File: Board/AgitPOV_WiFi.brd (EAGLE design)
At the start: 37.4 x 69.6 mm, 40 parts, among them U1 MMA8452Q

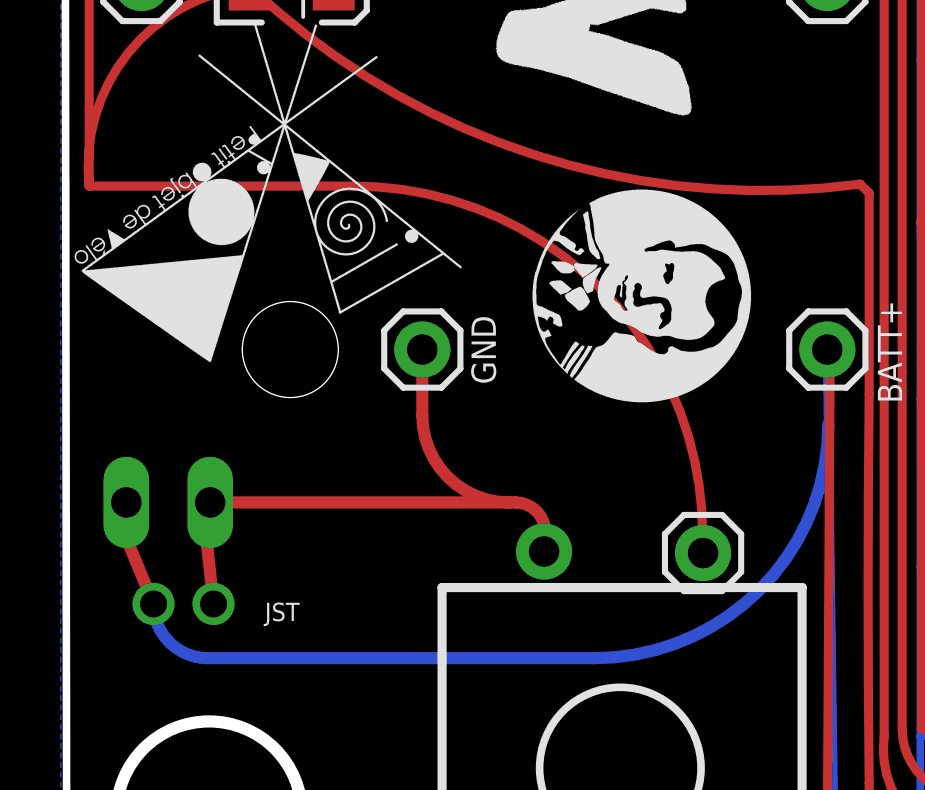
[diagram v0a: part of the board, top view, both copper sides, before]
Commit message: Cambios desde Manizales y Cartagena
- luz de colores en la pagina html
- individual AP desde el MAC address
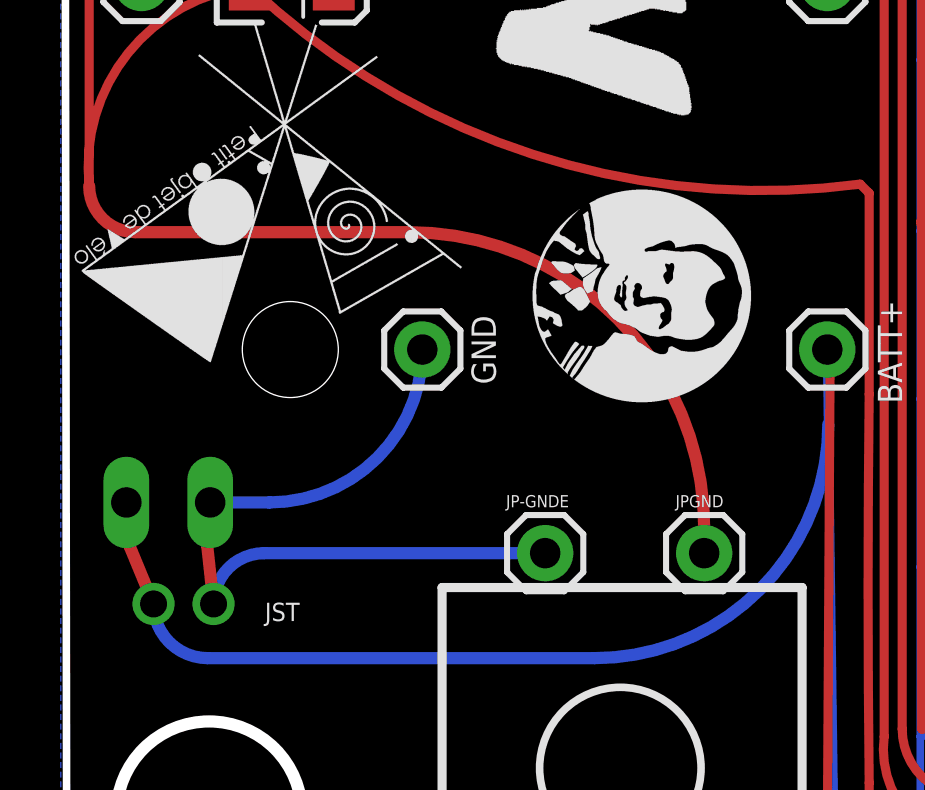
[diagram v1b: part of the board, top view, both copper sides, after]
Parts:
- removed JP-GND: SWITCH, SparkFun-Connectors:1X01
- added JPGND: switch, SparkFun-Connectors:1X01
- moved JP-GNDE 0.07 mm to (16.3, 13.9), flipped to the top
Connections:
- removed net GND1: JP-GND.1
- removed net N$65: U1.11
- removed net N$67: U1.9
- net ENTREEGND: now also JP-GNDE.1
- net GND: now also JPGND.1
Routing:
- net ENTREEGND: track 21.3 -> 24.3 mm
- net GND: track 394.7 -> 395.5 mm
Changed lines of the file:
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@@
 <layer number="17" name="Pads" color="2" fill="1" visible="yes" active="yes"/>
 <layer number="18" name="Vias" color="2" fill="1" visible="yes" active="yes"/>
-<layer number="19" name="Unrouted" color="6" fill="1" visible="yes" active="yes"/>
+<layer number="19" name="Unrouted" color="6" fill="1" visible="no" active="yes"/>
 <layer number="20" name="Dimension" color="15" fill="1" visible="yes" active="yes"/>
 <layer number="21" name="tPlace" color="14" fill="1" visible="yes" active="yes"/>
 <layer number="22" name="bPlace" color="13" fill="1" visible="yes" active="yes"/>
-<layer number="23" name="tOrigins" color="15" fill="1" visible="yes" active="yes"/>
-<layer number="24" name="bOrigins" color="15" fill="1" visible="yes" active="yes"/>
+<layer number="23" name="tOrigins" color="15" fill="1" visible="no" active="yes"/>
+<layer number="24" name="bOrigins" color="15" fill="1" visible="no" active="yes"/>
 <layer number="25" name="tNames" color="7" fill="1" visible="yes" active="yes"/>
-<layer number="26" name="bNames" color="7" fill="1" visible="yes" active="yes"/>
+<layer number="26" name="bNames" color="7" fill="1" visible="no" active="yes"/>
 <layer number="27" name="tValues" color="7" fill="1" visible="yes" active="yes"/>
-<layer number="28" name="bValues" color="7" fill="1" visible="yes" active="yes"/>
+<layer number="28" name="bValues" color="7" fill="1" visible="no" active="yes"/>
 <layer number="29" name="tStop" color="7" fill="3" visible="no" active="yes"/>
 <layer number="30" name="bStop" color="7" fill="6" visible="no" active="yes"/>
@@
 <element name="WEMOS2" library="SparkFun-Connectors" package="1X08_ROUND" value="Wemos D1 mini" x="2.84408125" y="50.6849625" smashed="yes" rot="R270">
 <attribute name="NAME" x="4.67288125" y="52.0311625" size="1.27" layer="25" ratio="10" rot="R270" display="off"/>
-<attribute name="VALUE" x="9.83608125" y="59.2519625" size="1.016" layer="28" rot="MR180"/>
+<attribute name="VALUE" x="9.83608125" y="59.2519625" size="1.016" layer="26" rot="MR180"/>
 </element>
 <element name="PIN0" library="SparkFun-Connectors" package="1X01" value="" x="25.80408125" y="2.4869625" smashed="yes">
@@
 <attribute name="VALUE" x="10.708" y="41.832" size="0.6096" layer="27" rot="SR0"/>
 </element>
-<element name="JP-GND" library="SparkFun-Connectors" package="1X01" value="SWITCH" x="21.5630375" y="13.90408125" smashed="yes" rot="R180">
-<attribute name="VALUE" x="23.6462375" y="10.44168125" size="0.8128" layer="26" rot="R270"/>
+<element name="JPGND" library="SparkFun-Connectors" package="1X01" value="switch" x="21.6" y="13.9" smashed="yes">
+<attribute name="NAME" x="20.6438" y="15.4288" size="0.4064" layer="25"/>
+<attribute name="VALUE" x="23.175" y="9.32" size="1.016" layer="27" rot="R270"/>
 </element>
-<element name="JP-GNDE" library="SparkFun-Connectors" package="1X01" value="" x="16.2630375" y="13.95408125" smashed="yes" rot="MR0">
-<attribute name="VALUE" x="17.5330375" y="10.77908125" size="1.27" layer="28" rot="MR0"/>
+<element name="JP-GNDE" library="SparkFun-Connectors" package="1X01" value="" x="16.3" y="13.9" smashed="yes">
+<attribute name="NAME" x="14.9938" y="15.4288" size="0.4064" layer="25"/>
+<attribute name="VALUE" x="15.03" y="10.725" size="1.27" layer="27"/>
 </element>
 </elements>
@@
 <wire x1="4.45" y1="49.75088125" x2="4.45" y2="52.82735625" width="0.4064" layer="1"/>
 <wire x1="4.45" y1="52.82735625" x2="5.00584375" y2="53.3832" width="0.4064" layer="1" curve="-90"/>
-<wire x1="1.1" y1="26.13548125" x2="9.91451875" y2="26.13548125" width="0.3048" layer="1"/>
-<wire x1="9.91451875" y1="26.13548125" x2="21.55" y2="14.5" width="0.3048" layer="1" curve="-90"/>
+<contactref element="JPGND" pad="1"/>
+<wire x1="1.1" y1="26.13548125" x2="2.63548125" y2="24.6" width="0.4064" layer="1" curve="90"/>
+<wire x1="2.63548125" y1="24.6" x2="11.75" y2="24.6" width="0.4064" layer="1"/>
+<wire x1="11.75" y1="24.6" x2="21.6" y2="14.75" width="0.4064" layer="1" curve="-90"/>
+<wire x1="21.6" y1="14.75" x2="21.6" y2="13.9" width="0.4064" layer="1"/>
 </signal>
 <signal name="N$6">
@@
 <wire x1="5.24511875" y1="12.2064375" x2="5.03251875" y2="14.1564375" width="0.4064" layer="1"/>
 <wire x1="5.03251875" y1="14.1564375" x2="5.13251875" y2="15.5904375" width="0.4064" layer="1"/>
-<wire x1="5.13251875" y1="15.5904375" x2="15.1" y2="15.5904375" width="0.4064" layer="1"/>
-<wire x1="15.1" y1="15.5904375" x2="15.3095625" y2="15.5904375" width="0.4064" layer="1"/>
-<wire x1="15.3095625" y1="15.5904375" x2="16.3" y2="14.6" width="0.4064" layer="1" curve="-90"/>
-<wire x1="12.20408125" y1="20.6869625" x2="12.20408125" y2="18.48635625" width="0.4064" layer="1"/>
-<wire x1="12.20408125" y1="18.48635625" x2="15.1" y2="15.5904375" width="0.4064" layer="1" curve="90"/>
+<contactref element="JP-GNDE" pad="1"/>
+<wire x1="12.20408125" y1="20.6869625" x2="7.10755625" y2="15.5904375" width="0.4064" layer="16" curve="-90"/>
+<wire x1="7.10755625" y1="15.5904375" x2="5.13251875" y2="15.5904375" width="0.4064" layer="16"/>
+<wire x1="5.24511875" y1="12.2064375" x2="6.93868125" y2="13.9" width="0.4064" layer="16" curve="-90"/>
+<wire x1="6.93868125" y1="13.9" x2="16.3" y2="13.9" width="0.4064" layer="16"/>
 </signal>
 <signal name="N$1">
@@
 <wire x1="17.8" y1="60.3" x2="25.70408125" y2="50.6849625" width="0.3048" layer="1" curve="-101.155894"/>
 </signal>
-<signal name="N$65">
-<contactref element="U1" pad="11"/>
-</signal>
-<signal name="N$67">
-<contactref element="U1" pad="9"/>
-</signal>
-<signal name="GND1">
-<contactref element="JP-GND" pad="1"/>
-</signal>
 </signals>

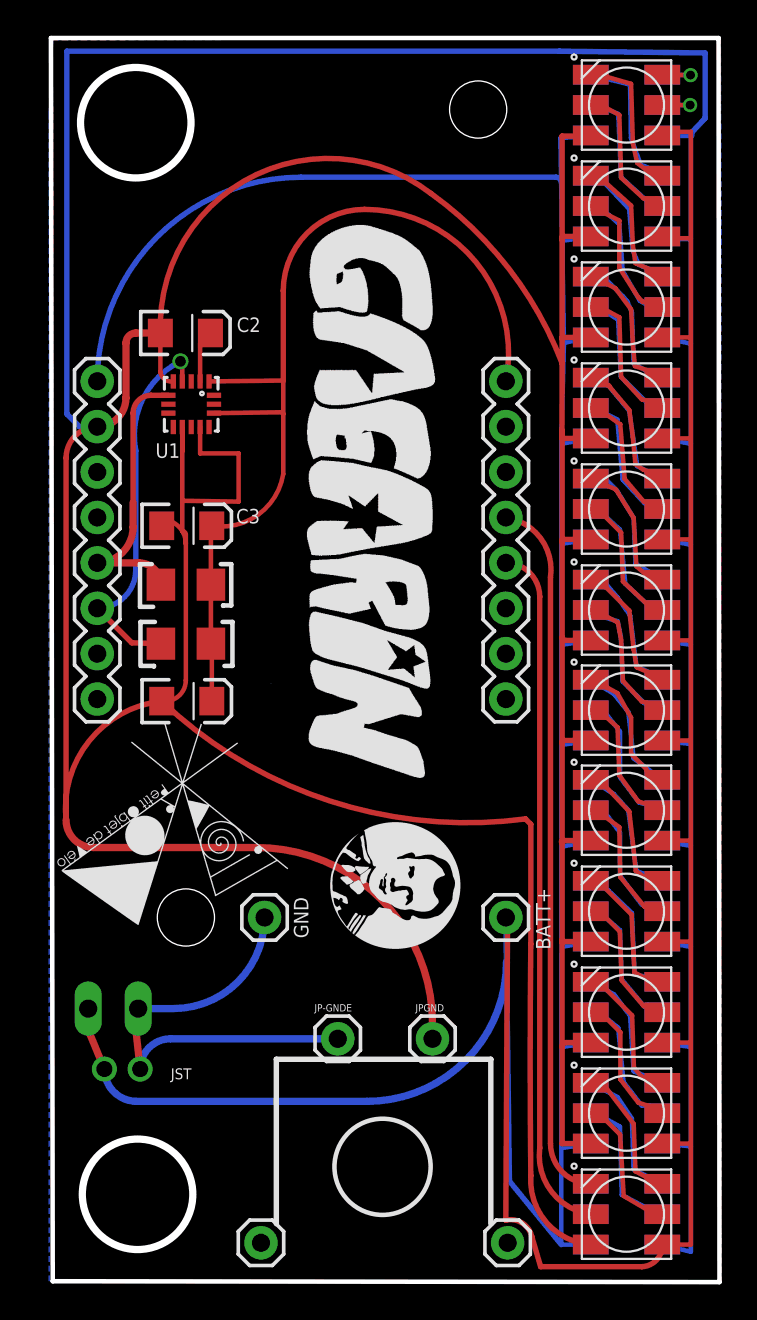
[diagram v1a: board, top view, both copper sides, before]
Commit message: Analysis and improvements to the lop
Implementation of spiffs accelerometer data saving (careful, there is a
200ms hit for every writing)
Scripts for gnuplot to analyze the data
Improvements to the low pass filter
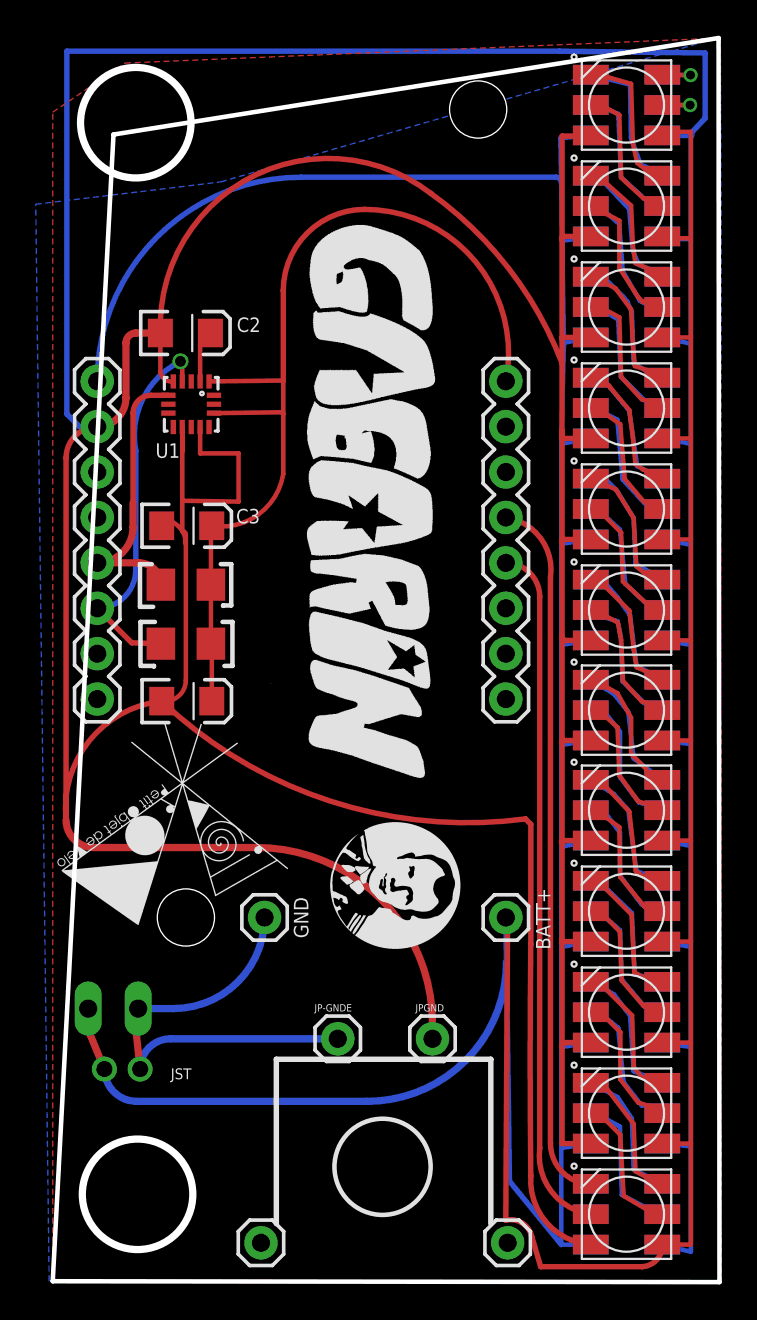
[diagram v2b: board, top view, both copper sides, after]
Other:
- board size 37.4 x 69.6 mm -> 37.3 x 69.6 mm
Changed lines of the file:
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@@
 <wire x1="27.40408125" y1="0.4869625" x2="15.40408125" y2="0.4869625" width="0.254" layer="22"/>
 <wire x1="15.40408125" y1="0.4869625" x2="10.40408125" y2="0.4869625" width="0.254" layer="22"/>
-<wire x1="0.35408125" y1="0.3369625" x2="0.25408125" y2="69.8869625" width="0.254" layer="20"/>
+<wire x1="0.35408125" y1="0.3369625" x2="3.75408125" y2="64.4869625" width="0.254" layer="20"/>
 <wire x1="0.35408125" y1="0.3369625" x2="37.65408125" y2="0.2869625" width="0.254" layer="20"/>
 <wire x1="15.40408125" y1="0.4869625" x2="15.4117" y2="4.406803125" width="0.254" layer="22"/>
@@
 <wire x1="15.6117" y1="4.606803125" x2="22.3117" y2="4.606803125" width="0.254" layer="22"/>
 <wire x1="22.3117" y1="4.606803125" x2="22.30408125" y2="0.5869625" width="0.254" layer="22"/>
-<wire x1="0.25408125" y1="69.8869625" x2="37.60408125" y2="69.8869625" width="0.254" layer="20"/>
+<wire x1="3.75408125" y1="64.4869625" x2="37.60408125" y2="69.8869625" width="0.254" layer="20"/>
 <wire x1="37.60408125" y1="69.8869625" x2="37.65408125" y2="0.2869625" width="0.254" layer="20"/>
 <hole x="24.15408125" y="65.8869625" drill="3.2"/>
@@
 <contactref element="WEMOS2" pad="2"/>
 <polygon width="0.6096" layer="1" isolate="0.3048" orphans="yes">
-<vertex x="0.30408125" y="69.7869625"/>
+<vertex x="4.40408125" y="68.4869625"/>
 <vertex x="37.70408125" y="69.8869625"/>
 <vertex x="37.75408125" y="0.3369625"/>
@@
 </polygon>
 <polygon width="0.254" layer="16" isolate="0.3048">
-<vertex x="0.35408125" y="69.7869625"/>
+<vertex x="9.75408125" y="61.8369625"/>
 <vertex x="37.70408125" y="69.9369625"/>
 <vertex x="37.75408125" y="58.6369625"/>
 <vertex x="37.60408125" y="0.2869625"/>
 <vertex x="0.15408125" y="0.3369625"/>
-<vertex x="0.15408125" y="65.6369625"/>
+<vertex x="-0.59591875" y="60.5869625"/>
 </polygon>
 <contactref element="DEL13" pad="6"/>
